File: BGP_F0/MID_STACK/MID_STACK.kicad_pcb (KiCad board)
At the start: 2 copper layers, 20 x 26 mm, 7 parts, among them P1 CONN_01X04, P2 CONN_01X09

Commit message: Mods and gerbers done
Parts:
- moved P2 0.60 mm to (171.2, 96.0)
- moved C2 0.10 mm to (183.4, 115.7)
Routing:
- net /MID_O: track 27.7 -> 28.8 mm
- net /VOL2: track 9.00 -> 9.67 mm
- net /MID_I: track 22.6 -> 22.0 mm
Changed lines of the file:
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@@
     (thickness 1.6)
     (drawings 8)
-    (tracks 46)
+    (tracks 44)
     (zones 0)
     (modules 7)
@@
     (visible_elements 7FFFFFFF)
     (pcbplotparams
-      (layerselection 0x010f0_80000001)
+      (layerselection 0x010fc_80000001)
       (usegerberextensions true)
       (usegerberattributes true)
@@
       (drillshape 0)
       (scaleselection 1)
-      (outputdirectory ../../GERBER/MID_0/))
+      (outputdirectory ../../GERBER/F0_MID/))
   )
   (net 0 "")
@@
   )
   (module LIBS:Potentiometer_Alpha_Tripple_Vertical_Dual_Shaft (layer B.Cu)
-    (at 171.25 95.4 90)
+    (at 171.25 96 90)
     (descr "Potentiometer, vertically mounted, Omeg PC16PU, Omeg PC16PU, Omeg PC16PU, Vishay/Spectrol 248GJ/249GJ Single, Vishay/Spectrol 248GJ/249GJ Single, Vishay/Spectrol 248GJ/249GJ Single, Vishay/Spectrol 248GH/249GH Single, Vishay/Spectrol 148/149 Single, Vishay/Spectrol 148/149 Single, Vishay/Spectrol 148/149 Single, Vishay/Spectrol 148A/149A Single with mounting plates, Vishay/Spectrol 148/149 Double, Vishay/Spectrol 148A/149A Double with mounting plates, Piher PC-16 Single, Piher PC-16 Single, Piher PC-16 Single, Piher PC-16SV Single, Piher PC-16 Double, Piher PC-16 Triple, Piher T16H Single, Piher T16L Single, Piher T16H Double, Alps RK163 Single, Alps RK163 Double, Alps RK097 Single, Alps RK097 Double, http://www.alps.com/prod/info/E/HTML/Potentiometer/RotaryPotentiometers/RK097/RK09712100AV.html")
     (tags "Potentiometer vertical  Omeg PC16PU  Omeg PC16PU  Omeg PC16PU  Vishay/Spectrol 248GJ/249GJ Single  Vishay/Spectrol 248GJ/249GJ Single  Vishay/Spectrol 248GJ/249GJ Single  Vishay/Spectrol 248GH/249GH Single  Vishay/Spectrol 148/149 Single  Vishay/Spectrol 148/149 Single  Vishay/Spectrol 148/149 Single  Vishay/Spectrol 148A/149A Single with mounting plates  Vishay/Spectrol 148/149 Double  Vishay/Spectrol 148A/149A Double with mounting plates  Piher PC-16 Single  Piher PC-16 Single  Piher PC-16 Single  Piher PC-16SV Single  Piher PC-16 Double  Piher PC-16 Triple  Piher T16H Single  Piher T16L Single  Piher T16H Double  Alps RK163 Single  Alps RK163 Double  Alps RK097 Single  Alps RK097 Double Dual Shaft")
@@
   )
   (module Capacitor_THT:C_Rect_L7.2mm_W2.5mm_P5.00mm_FKS2_FKP2_MKS2_MKP2 (layer B.Cu)
-    (at 183.3 115.7 90)
+    (at 183.4 115.7 90)
     (descr "C, Rect series, Radial, pin pitch=5.00mm, length*width=7.2*2.5mm^2, Capacitor, http://www.wima.com/EN/WIMA_FKS_2.pdf")
     (tags "C Rect series Radial pin pitch 5.00mm  length 7.2mm width 2.5mm Capacitor")
@@
   (gr_line (start 165 92) (end 165 118) (layer Edge.Cuts) (width 0.15))
   (gr_line (start 185 92) (end 165 92) (layer Edge.Cuts) (width 0.15))
-  (segment (start 166.7 97.1) (end 173.3 97.1) (width 0.4) (layer F.Cu) (net 1))
-  (segment (start 173.3 97.1) (end 175 95.4) (width 0.4) (layer F.Cu) (net 1))
+  (segment (start 172.8 98.2) (end 167.8 98.2) (width 0.4) (layer F.Cu) (net 1))
+  (segment (start 167.8 98.2) (end 166.7 97.1) (width 0.4) (layer F.Cu) (net 1))
+  (segment (start 175 96) (end 172.8 98.2) (width 0.4) (layer F.Cu) (net 1))
   (segment (start 166.7 102.1) (end 166.7 103.23137) (width 0.4) (layer F.Cu) (net 2))
   (segment (start 166.7 103.23137) (end 165.7 104.23137) (width 0.4) (layer F.Cu) (net 2))
@@
   (segment (start 168.2 109.4) (end 170.8 109.4) (width 0.4) (layer F.Cu) (net 2))
   (segment (start 170.8 109.4) (end 171.8 109.4) (width 0.4) (layer F.Cu) (net 2))
-  (segment (start 171.25 106) (end 171.25 101) (width 0.4) (layer B.Cu) (net 3))
-  (segment (start 171.3 101.05) (end 171.35 101) (width 0.4) (layer B.Cu) (net 3))
-  (segment (start 174 109.4) (end 174 108.7) (width 0.4) (layer F.Cu) (net 3))
-  (segment (start 174 108.7) (end 171.3 106) (width 0.4) (layer F.Cu) (net 3))
+  (segment (start 183.3 115.7) (end 182.4 116.6) (width 0.4) (layer F.Cu) (net 3))
+  (segment (start 182.4 116.6) (end 175.35 116.6) (width 0.4) (layer F.Cu) (net 3))
+  (segment (start 175.35 116.6) (end 174 115.25) (width 0.4) (layer F.Cu) (net 3))
+  (segment (start 174 115.25) (end 174 115) (width 0.4) (layer F.Cu) (net 3))
+  (segment (start 171.25 106) (end 171.25 104.727208) (width 0.4) (layer B.Cu) (net 3))
+  (segment (start 171.25 104.727208) (end 171.25 101) (width 0.4) (layer B.Cu) (net 3))
+  (segment (start 171.25 106) (end 174 108.75) (width 0.4) (layer F.Cu) (net 3))
+  (segment (start 174 108.75) (end 174 109.4) (width 0.4) (layer F.Cu) (net 3))
   (segment (start 171.3 106) (end 171.25 106) (width 0.4) (layer F.Cu) (net 3))
-  (segment (start 183.3 115.7) (end 182.16863 115.7) (width 0.4) (layer F.Cu) (net 3))
-  (segment (start 182.16863 115.7) (end 181.51862 116.35001) (width 0.4) (layer F.Cu) (net 3))
-  (segment (start 181.51862 116.35001) (end 175.10001 116.35001) (width 0.4) (layer F.Cu) (net 3))
-  (segment (start 175.10001 116.35001) (end 174 115.25) (width 0.4) (layer F.Cu) (net 3))
-  (segment (start 174 115.25) (end 174 115) (width 0.4) (layer F.Cu) (net 3))
   (segment (start 174 115) (end 174 109.4) (width 0.4) (layer F.Cu) (net 3))
   (segment (start 178 114.75) (end 178 115) (width 0.4) (layer B.Cu) (net 4))
+  (segment (start 176.9 108.85) (end 176.9 97.85) (width 0.4) (layer B.Cu) (net 5))
+  (segment (start 176.9 97.85) (end 178.75 96) (width 0.4) (layer B.Cu) (net 5))
   (segment (start 172 115) (end 172 113.75) (width 0.4) (layer B.Cu) (net 5))
-  (segment (start 172 113.75) (end 177.349999 108.400001) (width 0.4) (layer B.Cu) (net 5))
-  (segment (start 177.349999 96.800001) (end 177.850001 96.299999) (width 0.4) (layer B.Cu) (net 5))
-  (segment (start 177.349999 108.400001) (end 177.349999 96.800001) (width 0.4) (layer B.Cu) (net 5))
-  (segment (start 177.850001 96.299999) (end 178.75 95.4) (width 0.4) (layer B.Cu) (net 5))
+  (segment (start 172 113.75) (end 176.9 108.85) (width 0.4) (layer B.Cu) (net 5))
   (segment (start 172 115) (end 172 114.75) (width 0.4) (layer B.Cu) (net 5))
+  (segment (start 176 115) (end 176 116.25) (width 0.4) (layer B.Cu) (net 6))
+  (segment (start 176 116.25) (end 175.65 116.6) (width 0.4) (layer B.Cu) (net 6))
+  (segment (start 175.65 116.6) (end 171.249998 116.6) (width 0.4) (layer B.Cu) (net 6))
+  (segment (start 171.249998 116.6) (end 169.1 114.450002) (width 0.4) (layer B.Cu) (net 6))
+  (segment (start 169.1 114.450002) (end 169.1 98.15) (width 0.4) (layer B.Cu) (net 6))
+  (segment (start 169.1 98.15) (end 171.25 96) (width 0.4) (layer B.Cu) (net 6))
   (segment (start 176 115) (end 176 115.25) (width 0.4) (layer B.Cu) (net 6))
-  (segment (start 176 115.25) (end 174.899999 116.350001) (width 0.4) (layer B.Cu) (net 6))
-  (segment (start 170.350001 96.299999) (end 171.25 95.4) (width 0.4) (layer B.Cu) (net 6))
-  (segment (start 174.899999 116.350001) (end 170.999999 116.350001) (width 0.4) (layer B.Cu) (net 6))
-  (segment (start 170.999999 116.350001) (end 169.849999 115.200001) (width 0.4) (layer B.Cu) (net 6))
-  (segment (start 169.849999 115.200001) (end 169.849999 96.800001) (width 0.4) (layer B.Cu) (net 6))
-  (segment (start 169.849999 96.800001) (end 170.350001 96.299999) (width 0.4) (layer B.Cu) (net 6))
+  (segment (start 175 101) (end 178.75 101) (width 0.4) (layer F.Cu) (net 7))
+  (segment (start 170 103.1) (end 172.9 103.1) (width 0.4) (layer F.Cu) (net 7))
+  (segment (start 172.9 103.1) (end 175 101) (width 0.4) (layer F.Cu) (net 7))
+  (segment (start 168.2 104.9) (end 170 103.1) (width 0.4) (layer F.Cu) (net 7))
+  (segment (start 167 104.9) (end 168.2 104.9) (width 0.4) (layer F.Cu) (net 7))
   (segment (start 167 104.9) (end 167 104.75) (width 0.4) (layer F.Cu) (net 7))
-  (segment (start 167 104.75) (end 168.75 103) (width 0.4) (layer F.Cu) (net 7))
-  (segment (start 168.75 103) (end 172.4 103) (width 0.4) (layer F.Cu) (net 7))
-  (segment (start 174.100001 101.299999) (end 175 100.4) (width 0.4) (layer F.Cu) (net 7))
-  (segment (start 172.4 103) (end 174.100001 101.299999) (width 0.4) (layer F.Cu) (net 7))
-  (segment (start 178.75 100.4) (end 175 100.4) (width 0.4) (layer F.Cu) (net 7))
-  (segment (start 178.75 105.4) (end 175 105.4) (width 0.4) (layer F.Cu) (net 8))
-  (segment (start 183 104.9) (end 182 104.9) (width 0.4) (layer F.Cu) (net 8))
-  (segment (start 182 104.9) (end 181.5 105.4) (width 0.4) (layer F.Cu) (net 8))
-  (segment (start 181.5 105.4) (end 178.75 105.4) (width 0.4) (layer F.Cu) (net 8))
+  (segment (start 183 104.9) (end 179.85 104.9) (width 0.4) (layer F.Cu) (net 8))
+  (segment (start 179.85 104.9) (end 178.75 106) (width 0.4) (layer F.Cu) (net 8))
+  (segment (start 175 106) (end 178.75 106) (width 0.4) (layer F.Cu) (net 8))
   (zone (net 4) (net_name /Vref) (layer F.Cu) (hatch edge 0.508)
     (connect_pads (clearance 0.3))

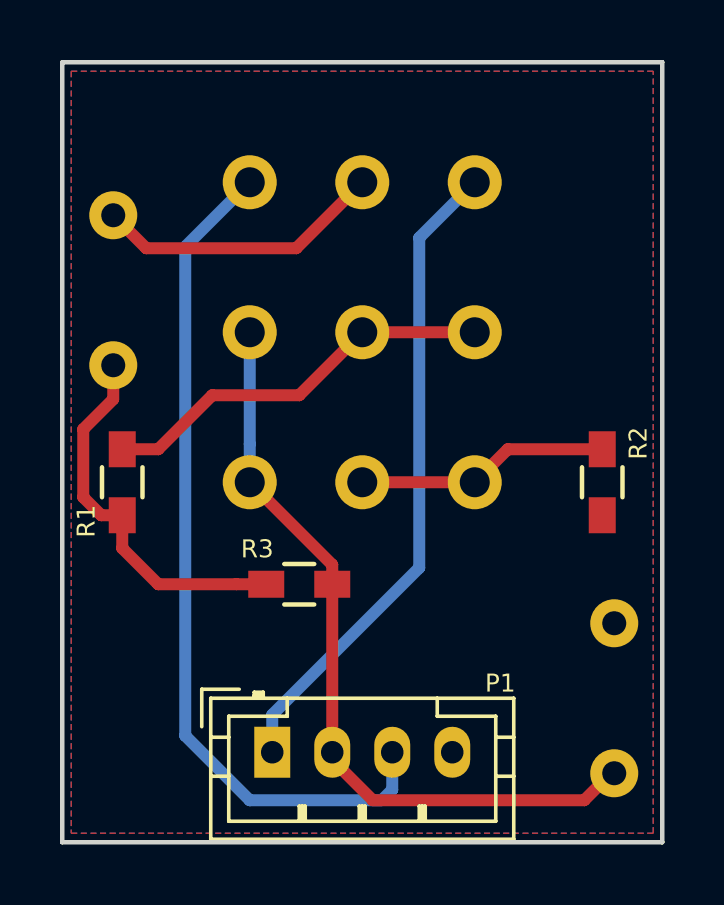
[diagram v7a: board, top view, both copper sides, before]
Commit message: F0 Mid Stack fixed
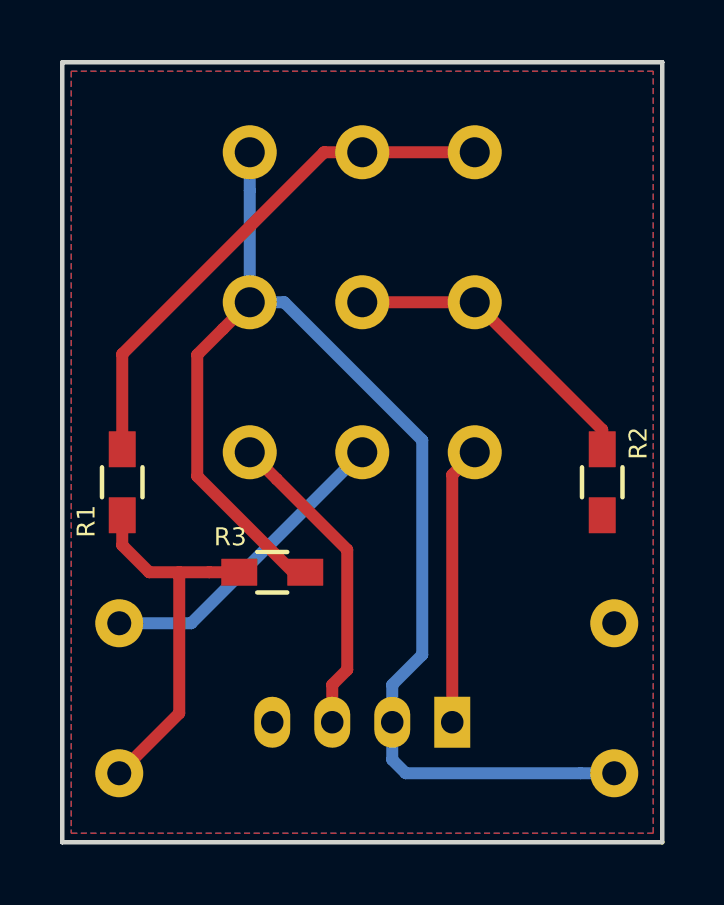
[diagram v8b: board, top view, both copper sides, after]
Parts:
- P1: moved to B.Cu
- moved C1 13.6 mm to (166.9, 110.7)
- moved P1 6.08 mm to (178.0, 114.0), turned to 180 degrees
- moved P2 1.00 mm to (171.2, 95.0)
- moved R3 0.98 mm to (172.0, 109.0)
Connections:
- P2 pad 1: /MID_O -> /F1_1
- P2 pad 2: /VOL2 -> /F1_2
- P2 pad 3: /MID_I -> /F1_2
- P2 pad 5: /F1_2 -> /F2_2
- P2 pad 6: /F1_2 -> /F2_2
- P2 pad 7: /F1_1 -> /MID_O
- P2 pad 8: /F2_2 -> /VOL2
- P2 pad 9: /F2_2 -> /MID_I
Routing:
- net /MID_O: track 28.8 -> 10.8 mm
- net /F1_1: track 25.7 -> 42.8 mm
- net /MID_I: track 22.0 -> 9.31 mm
- net /F1_2: track 13.5 -> 17.7 mm
- net /F2_2: track 8.46 -> 10.4 mm
- net /VOL2: track 9.67 -> 10.5 mm
